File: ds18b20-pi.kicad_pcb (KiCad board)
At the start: 2 copper layers, 62 x 56 mm, 14 parts, among them J1 Conn_01x03_Female, J10 Conn_01x03_Female, J2 Conn_01x03_Female, J3 Conn_01x03_Female, J4 Conn_01x03_Female, J5 Conn_01x03_Female, J6 Conn_01x03_Female, J7 Conn_01x03_Female, J8 Conn_01x03_Female, J9 Conn_01x03_Female, P1 CONN_13X2

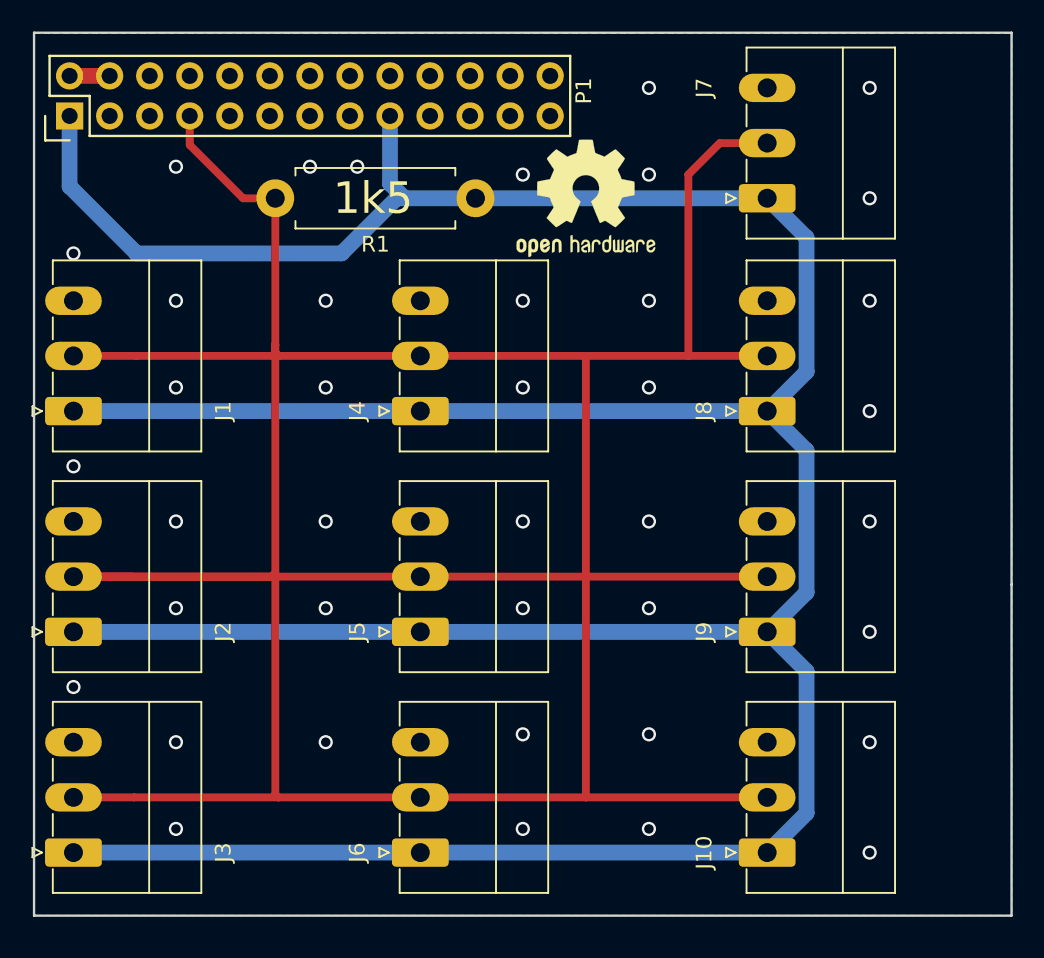
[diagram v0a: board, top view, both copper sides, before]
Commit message: Less GPIO4 more relays for motors
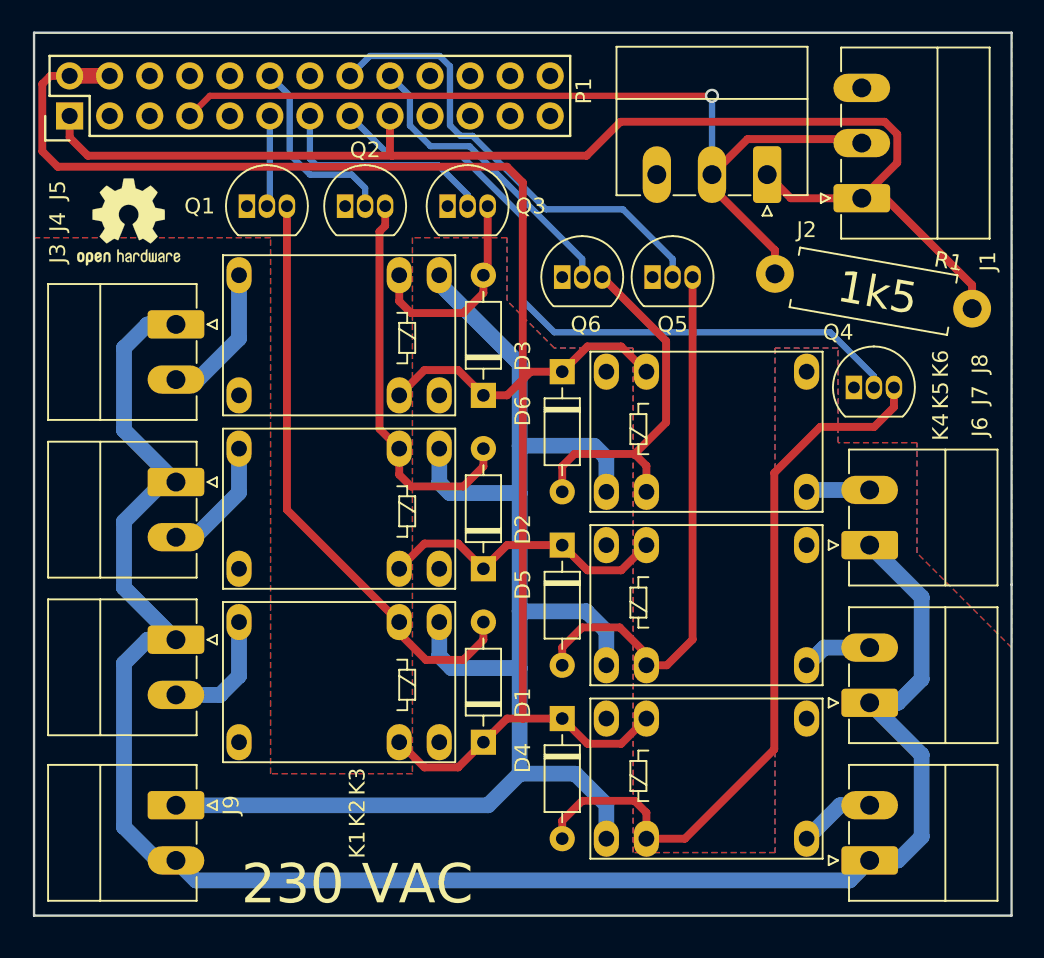
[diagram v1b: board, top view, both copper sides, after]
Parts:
- removed J10: Conn_01x03_Female, Connector_Phoenix_MC:PhoenixContact_MC_1,5_3-G-3.5_1x03_P3.50mm_Horizontal
- removed the REF** at (200.5, 170.5)
- removed the REF** at (178.5, 135.5)
- added D1: D, Diode_THT:D_DO-35_SOD27_P7.62mm_Horizontal, F.Cu at (172.0, 170.0)
- added D2: D, Diode_THT:D_DO-35_SOD27_P7.62mm_Horizontal, F.Cu at (172.0, 159.0)
- added D3: D, Diode_THT:D_DO-35_SOD27_P7.62mm_Horizontal, F.Cu at (172.0, 148.0)
- added D4: D, Diode_THT:D_DO-35_SOD27_P7.62mm_Horizontal, F.Cu at (177.0, 168.5)
- added D5: D, Diode_THT:D_DO-35_SOD27_P7.62mm_Horizontal, F.Cu at (177.0, 157.5)
- added D6: D, Diode_THT:D_DO-35_SOD27_P7.62mm_Horizontal, F.Cu at (177.0, 146.5)
- added K1: TIANBO-HJR-4102-L, Relay_THT:Relay_SPDT_HJR-4102, F.Cu at (156.5, 170.0)
- added K2: TIANBO-HJR-4102-L, Relay_THT:Relay_SPDT_HJR-4102, F.Cu at (156.5, 159.0)
- added K3: TIANBO-HJR-4102-L, Relay_THT:Relay_SPDT_HJR-4102, F.Cu at (156.5, 148.0)
- added K4: TIANBO-HJR-4102-L, Relay_THT:Relay_SPDT_HJR-4102, F.Cu at (192.5, 168.5)
- added K5: TIANBO-HJR-4102-L, Relay_THT:Relay_SPDT_HJR-4102, F.Cu at (192.5, 157.5)
- added K6: TIANBO-HJR-4102-L, Relay_THT:Relay_SPDT_HJR-4102, F.Cu at (192.5, 146.5)
- added Q1: 2N7000, Package_TO_SOT_THT:TO-92_Inline, F.Cu at (157.0, 136.0)
- added Q2: 2N7000, Package_TO_SOT_THT:TO-92_Inline, F.Cu at (163.2, 136.0)
- added Q3: 2N7000, Package_TO_SOT_THT:TO-92_Inline, F.Cu at (169.7, 136.0)
- added Q4: 2N7000, Package_TO_SOT_THT:TO-92_Inline, F.Cu at (195.5, 147.5)
- added Q5: 2N7000, Package_TO_SOT_THT:TO-92_Inline, F.Cu at (182.7, 140.5)
- added Q6: 2N7000, Package_TO_SOT_THT:TO-92_Inline, F.Cu at (177.0, 140.5)
- added REF**: KiCad-Logo2_6mm_SilkScreen, Symbol:KiCad-Logo2_6mm_SilkScreen, B.Cu at (188.0, 168.0)
- added REF**: OSHW-Logo2_7.3x6mm_SilkScreen, Symbol:OSHW-Logo2_7.3x6mm_SilkScreen, F.Cu at (149.5, 137.0)
- J3, J4, J5, J6, J7, J8, J9: value Conn_01x03_Female -> Conn_01x02_Female; footprint Connector_Phoenix_MC:PhoenixContact_MC_1,5_3-G-3.5_1x03_P3.50mm_Horizontal -> Connector_Phoenix_MC:PhoenixContact_MC_1,5_2-G-3.5_1x02_P3.50mm_Horizontal
- moved J2 52.7 mm to (190.0, 134.0), turned to 180 degrees
- moved J1 51.8 mm to (196.0, 135.5)
- moved J9 39.1 mm to (152.5, 174.0), turned to 270 degrees
- moved J7 32.7 mm to (196.5, 167.5)
- moved R1 32.3 mm to (203.0, 142.5), turned to 170 degrees
- moved J6 28.5 mm to (196.5, 177.5)
- moved J5 24.9 mm to (152.5, 143.5), turned to 270 degrees
- moved J4 16.1 mm to (152.5, 153.5), turned to 270 degrees
- moved J3 15.0 mm to (152.5, 163.5), turned to 270 degrees
- moved J8 10.7 mm to (196.5, 157.5)
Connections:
- J3 pad 1: +3V3 -> /N
- J3 pad 2: /GPIO4 -> Net-(J3-Pad2)
- J4 pad 1: +3V3 -> /N
- J4 pad 2: /GPIO4 -> Net-(J4-Pad2)
- J5 pad 1: +3V3 -> /N
- J5 pad 2: /GPIO4 -> Net-(J5-Pad2)
- J6 pad 1: +3V3 -> /N
- J6 pad 2: /GPIO4 -> Net-(J6-Pad2)
- J7 pad 1: +3V3 -> /N
- J7 pad 2: /GPIO4 -> Net-(J7-Pad2)
- J8 pad 1: +3V3 -> /N
- J8 pad 2: /GPIO4 -> Net-(J8-Pad2)
- J9 pad 1: +3V3 -> /L
- J9 pad 2: /GPIO4 -> /N
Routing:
- net /GPIO4: track 241.5 -> 57.1 mm, vias 0 -> 1
- net +3V3: track 237.4 -> 80.5 mm
- net +5V: track 2.54 -> 130.9 mm
- net /N: track 0.00 -> 118.2 mm
- net /L: track 0.00 -> 96.1 mm
- net Net-(D4-Pad2): track 0.00 -> 47.5 mm
- net /GPIO22: track 0.00 -> 43.9 mm
- net Net-(D1-Pad2): track 0.00 -> 37.7 mm
- net Net-(D5-Pad2): track 0.00 -> 35.0 mm
- net /GPIO23: track 0.00 -> 29.7 mm
- net Net-(D2-Pad2): track 0.00 -> 25.0 mm
- net Net-(D6-Pad2): track 0.00 -> 23.0 mm
- net /GPIO24: track 0.00 -> 19.3 mm
- net /GPIO21: track 0.00 -> 14.4 mm
- net Net-(D3-Pad2): track 0.00 -> 13.4 mm
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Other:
- net class Logic_GPIO added: clearance 0.2, trace_width 0.4, via_dia 0.9, via_drill 0.6
- net class Logic_Power added: clearance 0.2, trace_width 0.5, via_dia 0.9, via_drill 0.6
- net class Power: clearance 0.2 -> 1
- board text added: "230 VAC"
- board text added: "Raspberry Pi 1 DS18B20 Rev. B"
- board text added: "black"
- board text added: "github.com/ schotter/ ds18b20-pi"
- board text added: "red"
- board text added: "yellow"
- board text removed: "Raspberry Pi 1 DS18B20 Rev. A"
- board text removed: "gelb"
- board text removed: "github.com/schotter/ds18b20-pi"
- board text removed: "rot"
- board text removed: "schwarz"

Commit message: More Vias and more GND
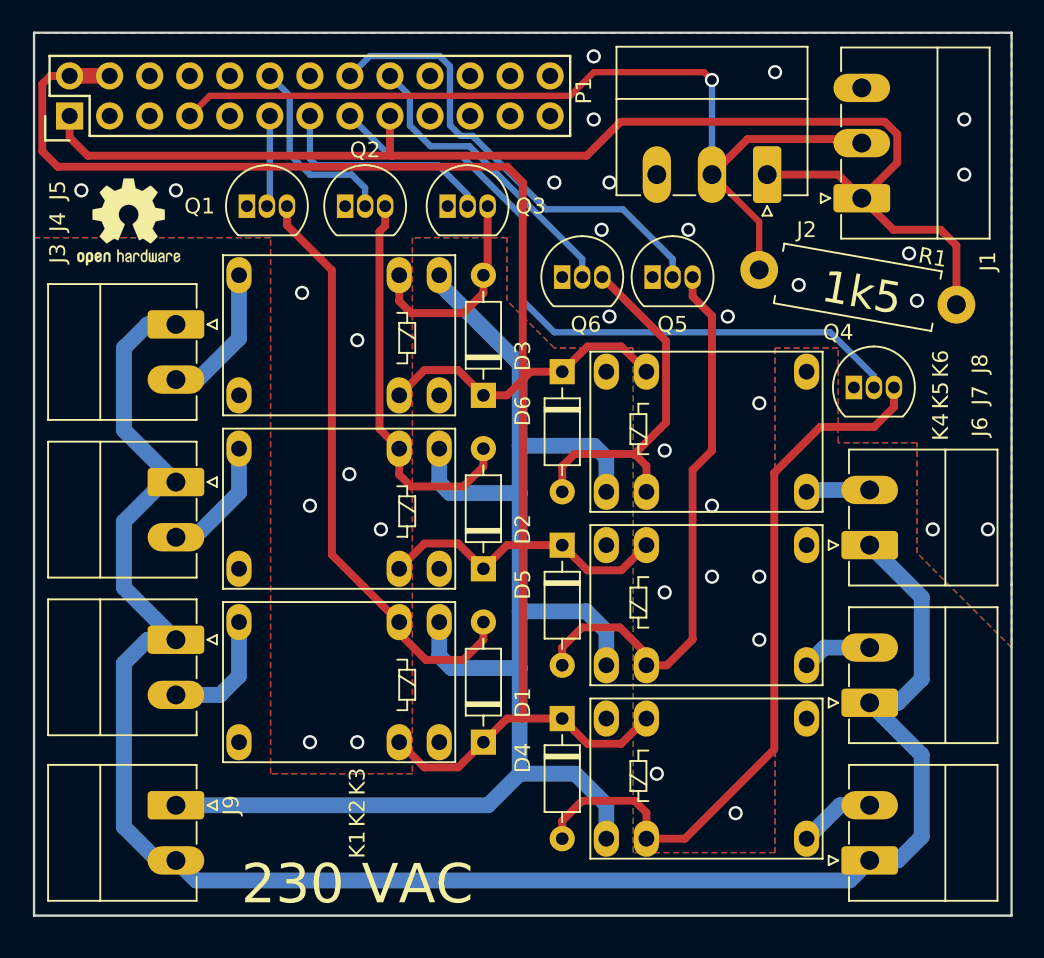
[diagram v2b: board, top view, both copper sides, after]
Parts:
- moved R1 1.03 mm to (202.0, 142.2)
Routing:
- net /GPIO4: track 57.1 -> 59.1 mm
- net Net-(D5-Pad2): track 35.0 -> 36.0 mm
- net GND: vias 0 -> 34

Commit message: Indicator led for each relay
There are leds that already have a series resistor included to limit the
current. Those leds are necessary for this board, because there is not
enough space for addition resistors.
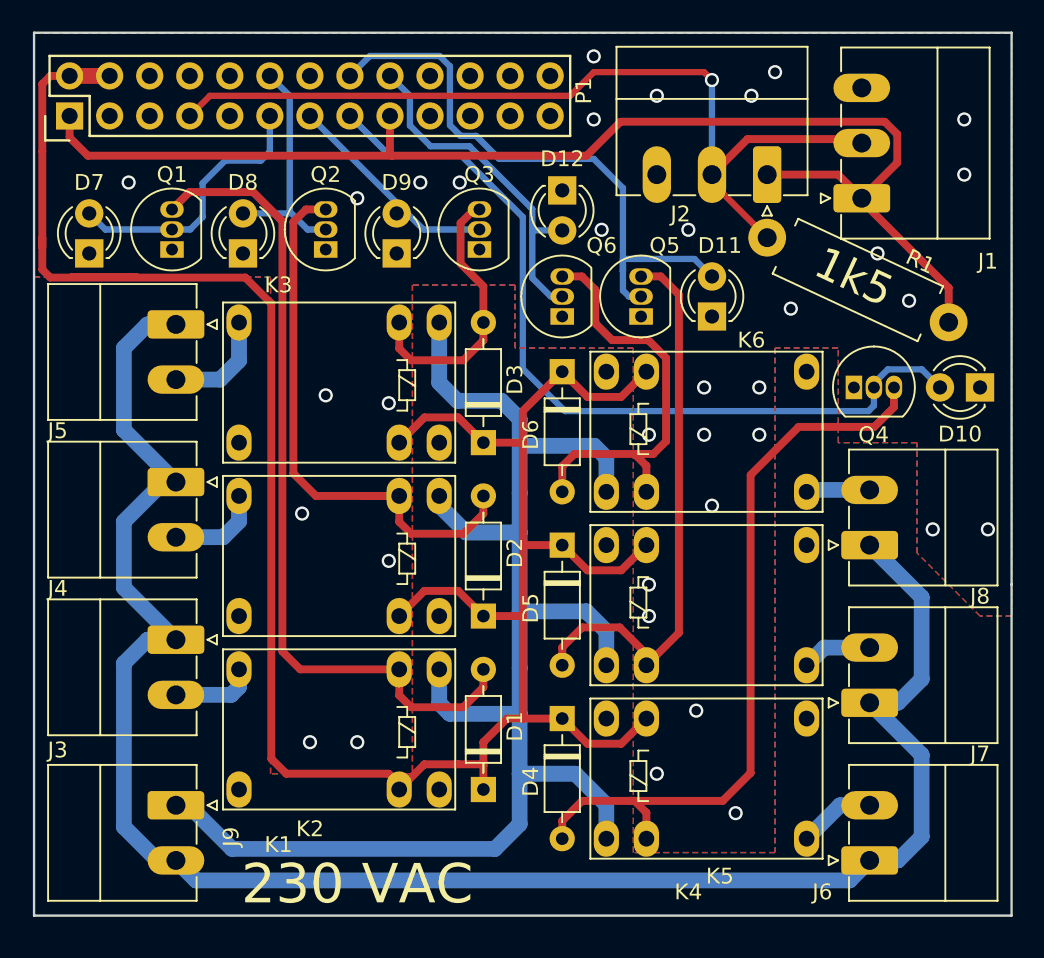
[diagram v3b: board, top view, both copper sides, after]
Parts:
- removed REF**: KiCad-Logo2_6mm_SilkScreen, Symbol:KiCad-Logo2_6mm_SilkScreen
- removed REF**: OSHW-Logo2_7.3x6mm_SilkScreen, Symbol:OSHW-Logo2_7.3x6mm_SilkScreen
- added D10: LED, LED_THT:LED_D3.0mm, F.Cu at (203.5, 147.5)
- added D11: LED, LED_THT:LED_D3.0mm, F.Cu at (186.5, 143.0)
- added D12: LED, LED_THT:LED_D3.0mm, F.Cu at (177.0, 135.0)
- added D7: LED, LED_THT:LED_D3.0mm, F.Cu at (147.0, 139.0)
- added D8: LED, LED_THT:LED_D3.0mm, F.Cu at (156.8, 139.0)
- added D9: LED, LED_THT:LED_D3.0mm, F.Cu at (166.5, 139.0)
- moved Q1 5.49 mm to (152.2, 138.8), turned to 90 degrees
- moved Q3 3.41 mm to (171.8, 138.8), turned to 90 degrees
- moved Q2 3.01 mm to (162.0, 138.8), turned to 90 degrees
- moved D1 3.00 mm to (172.0, 173.0)
- moved D2 3.00 mm to (172.0, 162.0)
- moved D3 3.00 mm to (172.0, 151.0)
- moved K1 3.00 mm to (156.5, 173.0)
- moved K2 3.00 mm to (156.5, 162.0)
- moved K3 3.00 mm to (156.5, 151.0)
- moved Q5 2.60 mm to (182.0, 143.0), turned to 90 degrees
- moved Q6 2.50 mm to (177.0, 143.0), turned to 90 degrees
- moved R1 1.22 mm to (201.5, 143.4), turned to 155 degrees
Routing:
- net +5V: track 130.9 -> 152.9 mm
- net Net-(D1-Pad2): track 37.7 -> 52.3 mm
- net Net-(D2-Pad2): track 25.0 -> 36.9 mm
- net /GPIO17: track 5.80 -> 17.4 mm
- net /GPIO22: track 43.9 -> 53.2 mm
- net /GPIO23: track 29.7 -> 37.9 mm
- net Net-(D3-Pad2): track 13.4 -> 17.4 mm
- net Net-(D6-Pad2): track 23.0 -> 26.8 mm
- net /GPIO24: track 19.3 -> 22.3 mm
- net Net-(J3-Pad2): track 7.92 -> 5.33 mm
- net /GPIO18: track 12.3 -> 14.9 mm
- net Net-(J5-Pad2): track 9.10 -> 6.92 mm
- net Net-(J4-Pad2): track 7.97 -> 6.03 mm
- net /GPIO4: track 59.1 -> 57.3 mm
- net /L: track 96.1 -> 97.7 mm
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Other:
- board text added: "Raspberry Pi 1 DS18B20 Rev. C"
- board text removed: "Raspberry Pi 1 DS18B20 Rev. B"

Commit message: oshw logo
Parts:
- added REF**: OSHW-Logo2_7.3x6mm_SilkScreen, Symbol:OSHW-Logo2_7.3x6mm_SilkScreen, B.Cu at (194.0, 141.5)

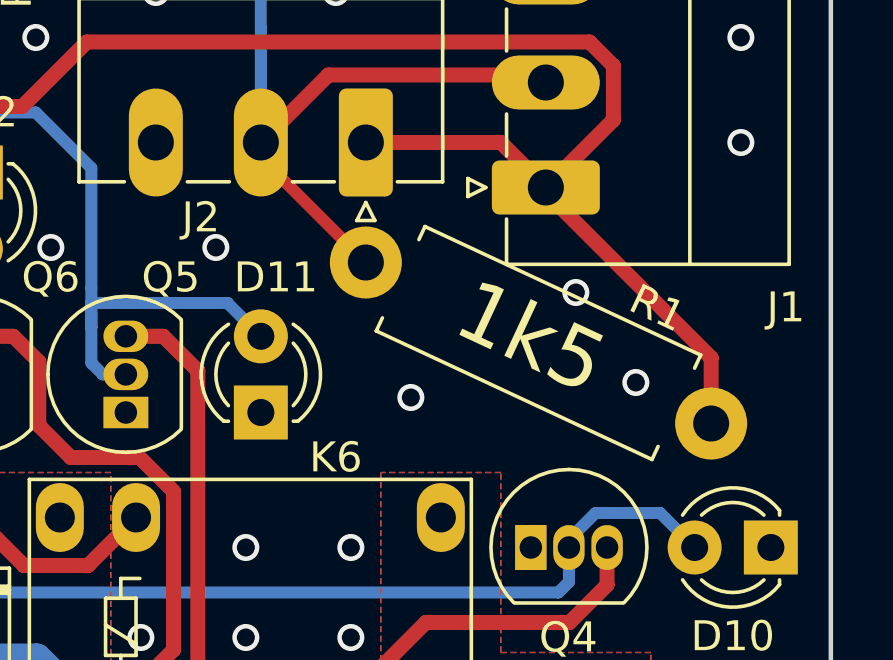
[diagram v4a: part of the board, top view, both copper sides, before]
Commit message: tvs diode
The sensors are connected through long wires, which make it very likely
for radiation to couple into them and disturb the communication.
Therefore a tvs diode was added. Unfortunately for a breakdown voltage
of 3,3V there are only smd packages available.
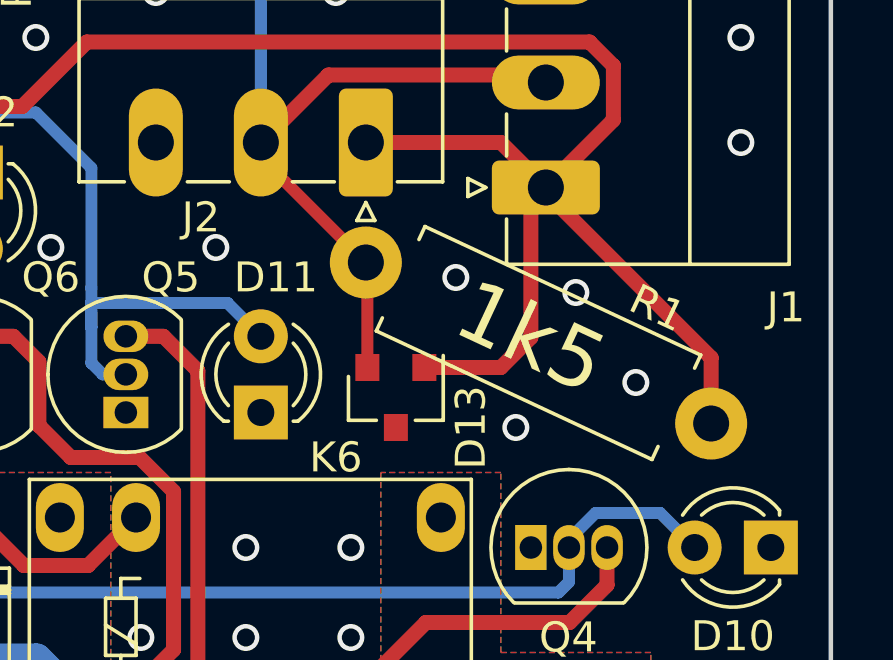
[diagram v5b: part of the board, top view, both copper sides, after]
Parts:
- added D13: PESD3V3S2UT, Package_TO_SOT_SMD:SOT-23, F.Cu at (191.0, 142.5)
- moved REF** 30.8 mm to (187.0, 171.5), turned to 90 degrees
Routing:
- net +3V3: track 79.9 -> 89.1 mm
- net /GPIO4: track 57.3 -> 60.8 mm
- net GND: vias 35 -> 36
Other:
- board text added: "Raspberry Pi 1 DS18B20 Rev. D"
- board text removed: "Raspberry Pi 1 DS18B20 Rev. C"
